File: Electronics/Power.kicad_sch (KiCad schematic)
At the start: 71 parts, among them IC1 TPS65251-1RHAR, IC2 MAX20008AFOC_VY+T, U6 AMS1117-3.3

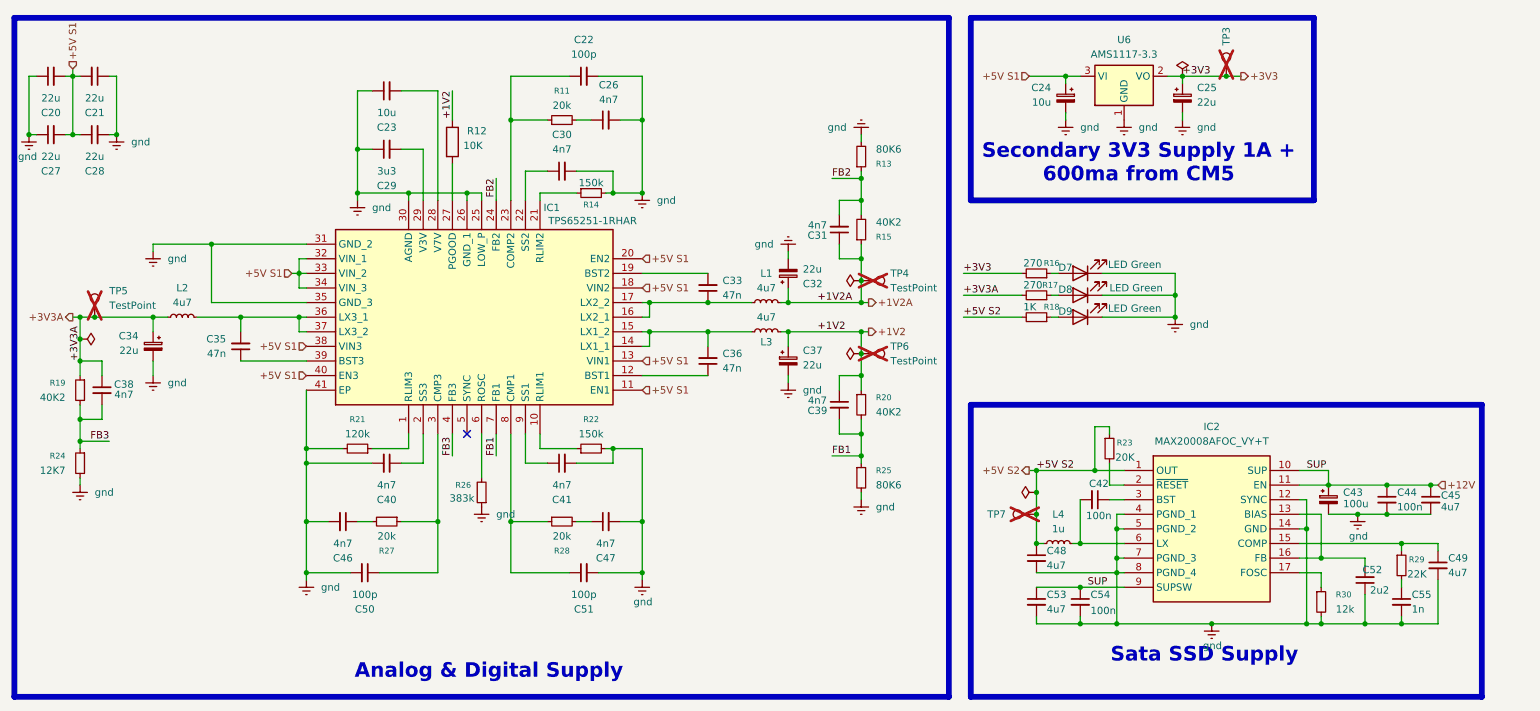
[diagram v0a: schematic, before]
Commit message: Power symbols changed and sata hub fixed schem
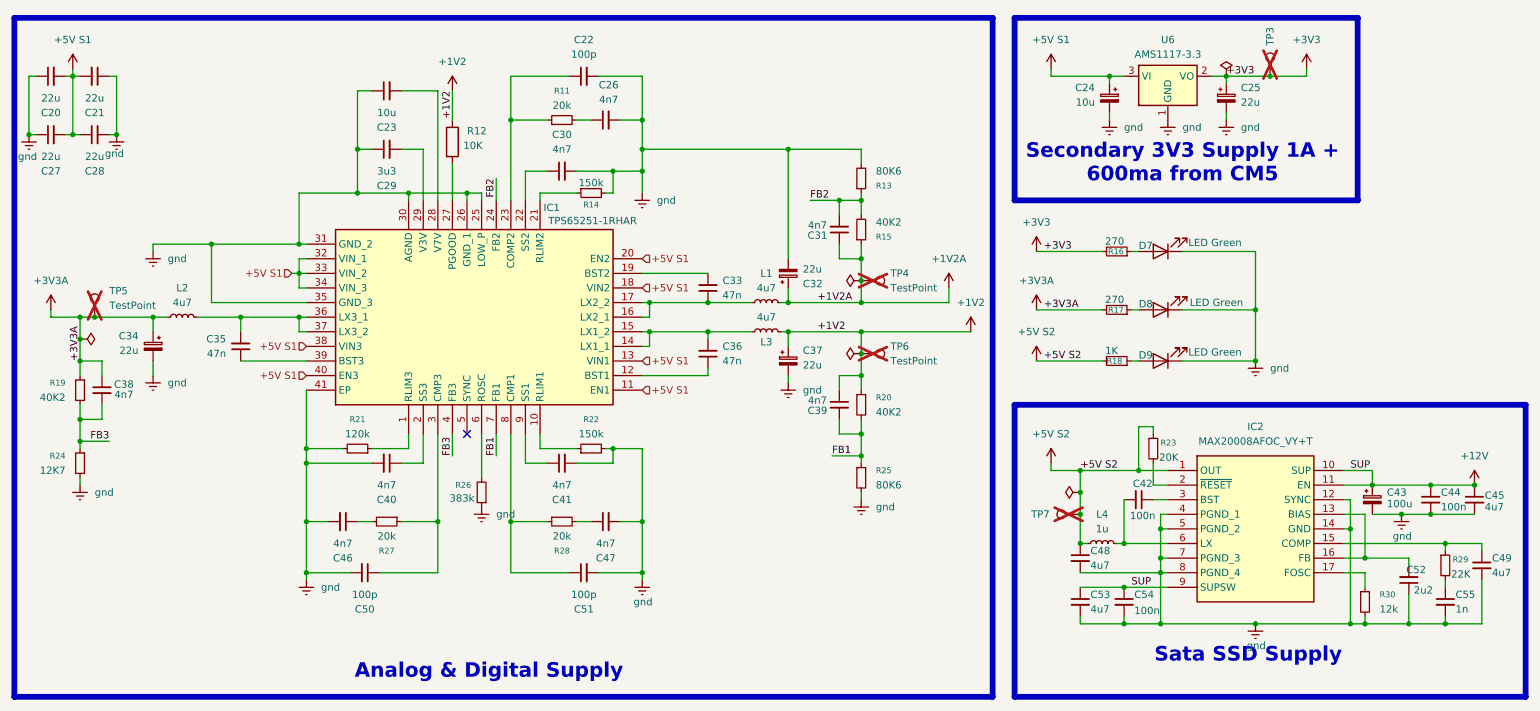
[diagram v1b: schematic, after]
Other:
- moved on the sheet: C24, C25, C36, C42, C43, C44, C45, C48, C49, C52, C53, C54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
